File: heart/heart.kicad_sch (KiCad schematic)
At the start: 47 parts

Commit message: [New] Almost complete heart board
Signed-off-by: Homalozoa X <nx.tardis@gmail.com>
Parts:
- added C1, C2: 30pf 10V, Capacitor_SMD:C_0805_2012Metric, symbol Device:C
- added C21, C23: 1uf 10V, Capacitor_SMD:C_0402_1005Metric, symbol Device:C
- added C22, C24: 470pf 10V, Capacitor_SMD:C_0402_1005Metric, symbol Device:C
- added C25, C26: 22nf 10V, Capacitor_SMD:C_0805_2012Metric, symbol Device:C
- added C27: 1nf 2kv, Capacitor_SMD:C_1206_3216Metric, symbol Device:C
- added C28, C29: 4.7nf 2kv, Capacitor_SMD:C_1206_3216Metric, symbol Device:C
- added FB1: 220R, symbol Device:FerriteBead
- added J10: UART_FLASH_ESP, Connector_JST:JST_GH_BM05B-GHS-TBT_1x05-1MP_P1.25mm_Vertical, symbol Connector:Conn_01x05_Female
- added J11: RJ45_LED_Shielded, symbol Connector:RJ45_LED_Shielded
- added Q4, Q5, Q6: FH1404G6, Rolling_Custom:PDFN5X6-8L, symbol Rolling_Custom:WNM6006
- added R10, R11, R12, R13, R14, R33, R6, R7, R8, R9: 0r, Resistor_SMD:R_0402_1005Metric, symbol Device:R_US
- added R15: 499r, Resistor_SMD:R_0402_1005Metric, symbol Device:R_US
- added R22, R23: 10k, Resistor_SMD:R_0402_1005Metric, symbol Device:R_US
- added R24: 12.1k, Resistor_SMD:R_0201_0603Metric, symbol Device:R_US
- added R25, R26, R27, R28: 49.9r, Resistor_SMD:R_0402_1005Metric, symbol Device:R_US
- added R29, R30: 75r, Resistor_SMD:R_0402_1005Metric, symbol Device:R_US
- added R3: 33r, Resistor_SMD:R_0402_1005Metric, symbol Device:R_US
- added R31, R32: 332r, Resistor_SMD:R_0402_1005Metric, symbol Device:R_US
- added R5: 470r, Resistor_SMD:R_0402_1005Metric, symbol Device:R_US
- added T1: H1102NLT, Rolling_Custom:XFMR_H1102NLT, symbol Rolling_Custom:H1102NLT
- added U4: LAN8720A, Package_DFN_QFN:QFN-24-1EP_4x4mm_P0.5mm_EP2.6x2.6mm, symbol Interface_Ethernet:LAN8720A
- added Y1: 25MHz, Crystal:Crystal_SMD_3225-4Pin_3.2x2.5mm, symbol Device:Crystal_GND24
- C3, C4: renamed from C?; footprint Capacitor_SMD:C_0805_2012Metric -> Capacitor_SMD:C_0402_1005Metric
- C5: renamed from C?; value 100uf 10V -> 100uf 6.3V
- gave numbers to parts that had none: 44
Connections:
- net +24V: now also Q4.5; no longer J1.1 (VBUS), J2.1 (VBUS), J3.1 (VBUS), J4.1 (VBUS), J5.1 (VBUS), J6.1 (VBUS), J7.1 (VBUS)
- net +3V3: now also C21.2, C22.2, FB1.1, U4.9 (VDDIO)
- net BOOT0: now also R5.1
- net ESP_DTR: now also J10.1 (Pin_1)
- net ESP_RTS: now also J10.2 (Pin_2)
- net ESP_RXD: now also J10.4 (Pin_4)
- net ESP_TXD: now also R15.2
- net GND: now also J9.2 (-), J9.S1 (SHIELD), J9.S2 (SHIELD), C1.1, C2.1, C21.1, C22.1, C23.1, C24.1, C25.1, C26.1, C28.1, C29.1, J10.5 (Pin_5), J11.11, J11.9, R22.2, R23.2, R24.2, U4.25 (VSS), Y1.2, Y1.4
- net TCAN_INT: now also U1.4 (SENSOR_VP/GPIO36/ADC1_CH0)
- net TCAN_RST: now also U1.26 (ADC2_CH0/GPIO4)
- net TCAN_WKRQ: now also U1.5 (SENSOR_VN/GPIO39/ADC1_CH3)
- net at U1.10 (DAC_1/ADC2_CH8/GPIO25): now also R12.2
- net at U1.11 (DAC_2/ADC2_CH9/GPIO26): now also R13.2
- net at U1.12 (ADC2_CH7/GPIO27): now also R14.2
- net at U1.29 (GPIO5): now also R6.2
- net at U1.30 (GPIO18): now also R7.2
- net at U1.31 (GPIO19): now also R8.2
- net at U1.33 (GPIO21): now also R9.2
- net at U1.36 (GPIO22): now also R10.2
- net at U1.37 (GPIO23): now also R11.2
- net PWRCT_1: now reaches U1.6 (GPIO34/ADC1_CH6)
- net PWRCT_1: now also Q4.4
- net PWRCT_2: now reaches U1.7 (GPIO35/ADC1_CH7)
- net PWRCT_2: now also Q5.4
- net PWRCT_3: now reaches U1.8 (32K_XP/GPIO32/ADC1_CH4)
- net PWRCT_3: now also Q6.4
- net ETH_RXER: now reaches U1.9 (32K_XN/GPIO33/ADC1_CH5)
- net ETH_RXER: now also U4.10 (RXER/PHYAD0)
- net EXT_PWR: now reaches J9.1 (+)
- net EXT_PWR: now also Q5.5, Q6.1, Q6.2, Q6.3
- new net: C27.2, R29.1, R30.1
- new net: R29.2, T1.10
- new net: R3.2, U4.14 (INT/REFCLKO)
- new net: R24.1, U4.24 (RBIAS)
- new net: J11.12, R31.1
- new net: J11.1, T1.16
- new net: J11.10, R32.1
- new net: J11.2, T1.14
- new net: J11.3, T1.11
- new net: J11.6, T1.9
- new net: J10.3 (Pin_3), R15.1
- new net: C26.2, T1.7
- new net: C25.2, T1.2
- new net: R30.2, T1.15
- new net ETH_CLKI: C1.2, U4.5 (XTAL1/CLKIN), Y1.1
- new net ETH_CLKO: C2.2, U4.4 (XTAL2), Y1.3
- new net ETH_LED1: R22.1, R31.2, U4.3 (LED1/REGOFF)
- new net ETH_LED2: R23.1, R32.2, U4.2 (LED2/nINTSEL)
- new net ETH_MDC: R11.1, U4.13 (MDC)
- new net ETH_MDIO: R7.1, U4.12 (MDIO)
- new net ETH_RST_N: R6.1, U4.15 (RST)
- new net ETH_RXN: R25.1, T1.8, U4.22 (RXN)
- new net ETH_RXP: R26.1, T1.6, U4.23 (RXP)
- new net ETH_TXN: R27.1, T1.3, U4.20 (TXN)
- new net ETH_TXP: R28.1, T1.1, U4.21 (TXP)
- new net GNDPWR: C27.1, C28.2, C29.2, R33.2
- new net GNDS: J11.SH, R33.1
- new net PWR_EXPORT: J1.1 (VBUS), J2.1 (VBUS), J3.1 (VBUS), J4.1 (VBUS), J5.1 (VBUS), J6.1 (VBUS), J7.1 (VBUS), Q4.1, Q4.2, Q4.3, Q5.1, Q5.2, Q5.3, Q6.5
- new net RMII_CRS_DV: R14.1, U4.11 (CRS_DV/MODE2)
- new net RMII_REF_CLK: R3.1, R5.2
- new net RMII_RXD0: R12.1, U4.8 (RXD0/MODE0)
- new net RMII_RXD1: R13.1, U4.7 (RXD1/MODE1)
- new net RMII_TXD0: R8.1, U4.17 (TXD0)
- new net RMII_TXD1: R10.1, U4.18 (TXD1)
- new net RMII_TX_EN: R9.1, U4.16 (TXEN)
- new net VDDA: FB1.2, R25.2, R26.2, R27.2, R28.2, U4.1 (VDD2A), U4.19 (VDD1A)
- new net VDDCR: C23.2, C24.2, U4.6 (VDDCR)
- no-connect marks 4 -> 6
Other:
- moved on the sheet: C10, C13, C14, C16, C17, C18, C3, C4, C5, C6, C8, C9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

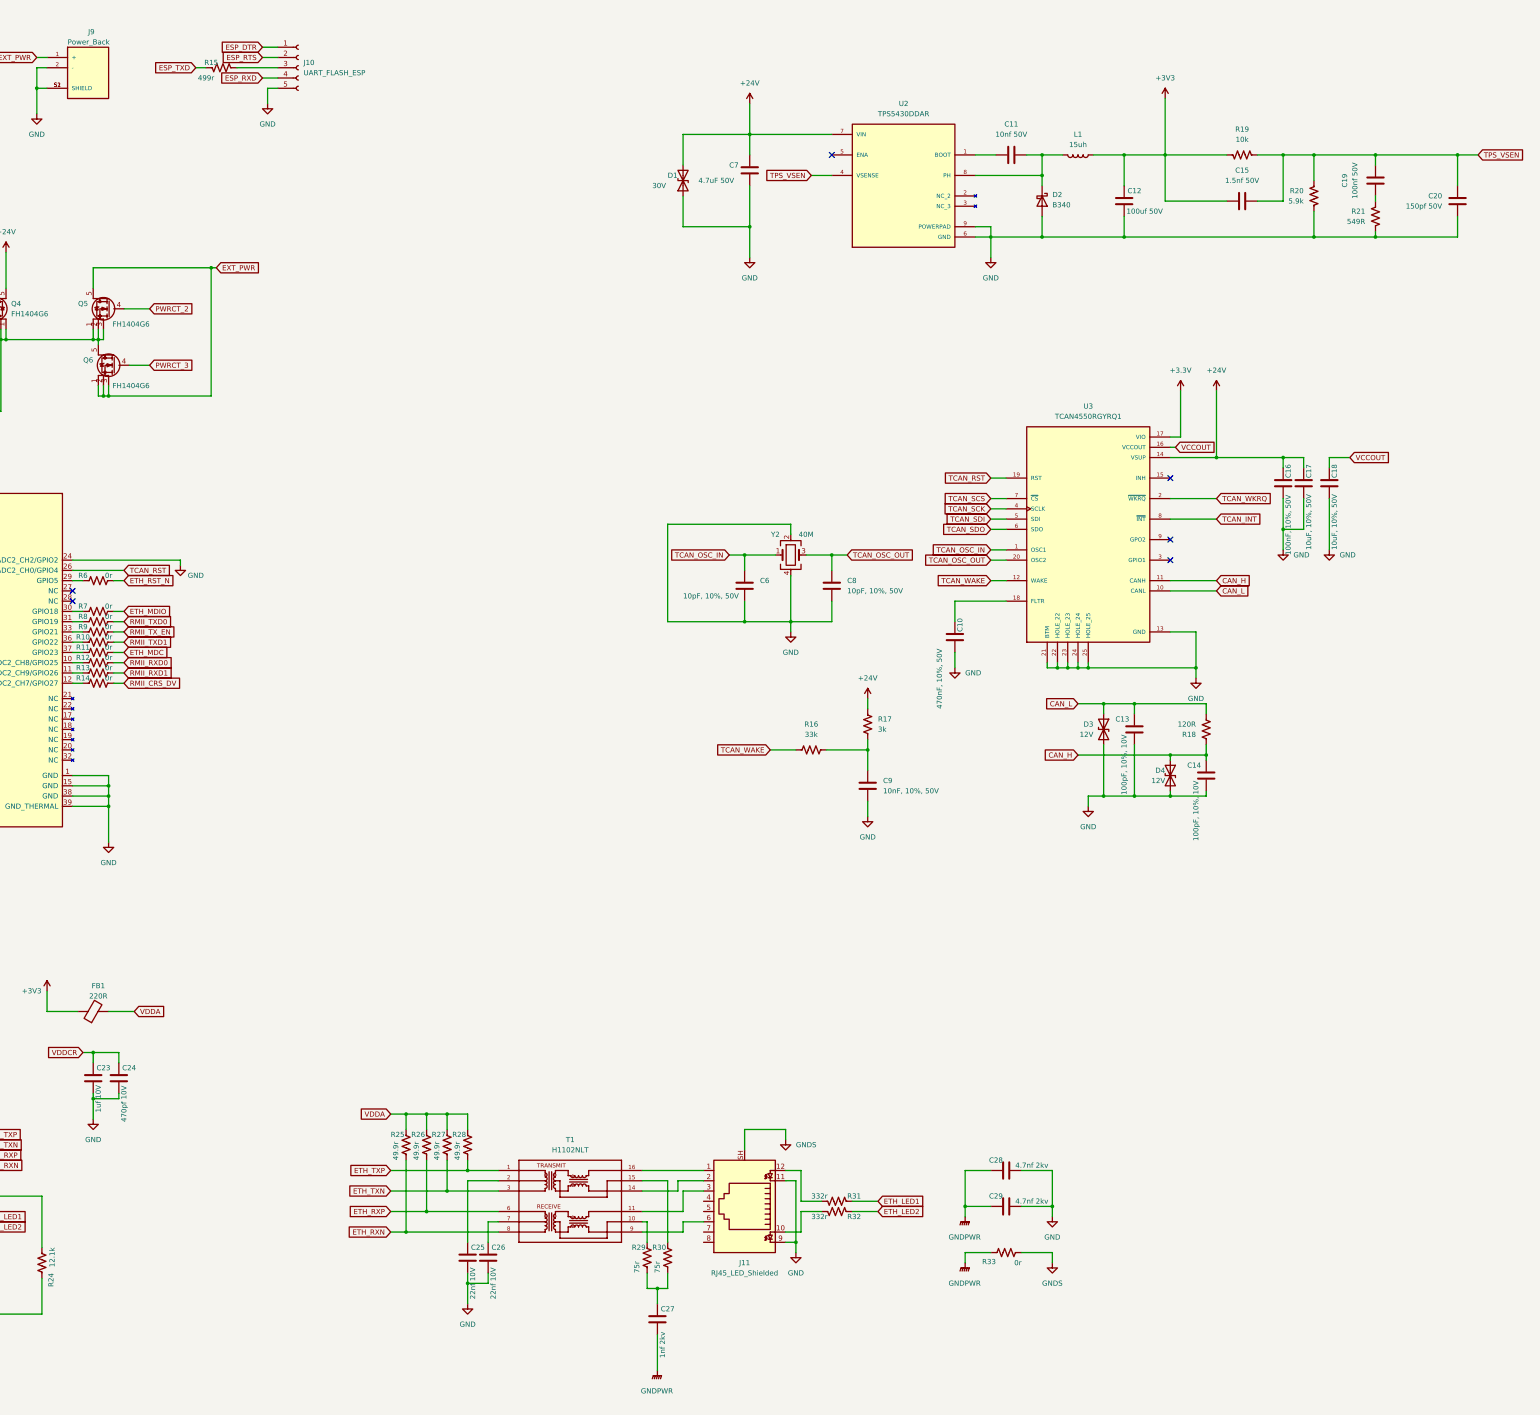
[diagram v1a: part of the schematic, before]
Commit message: [New] Complete heart board
Signed-off-by: Homalozoa X <nx.tardis@gmail.com>
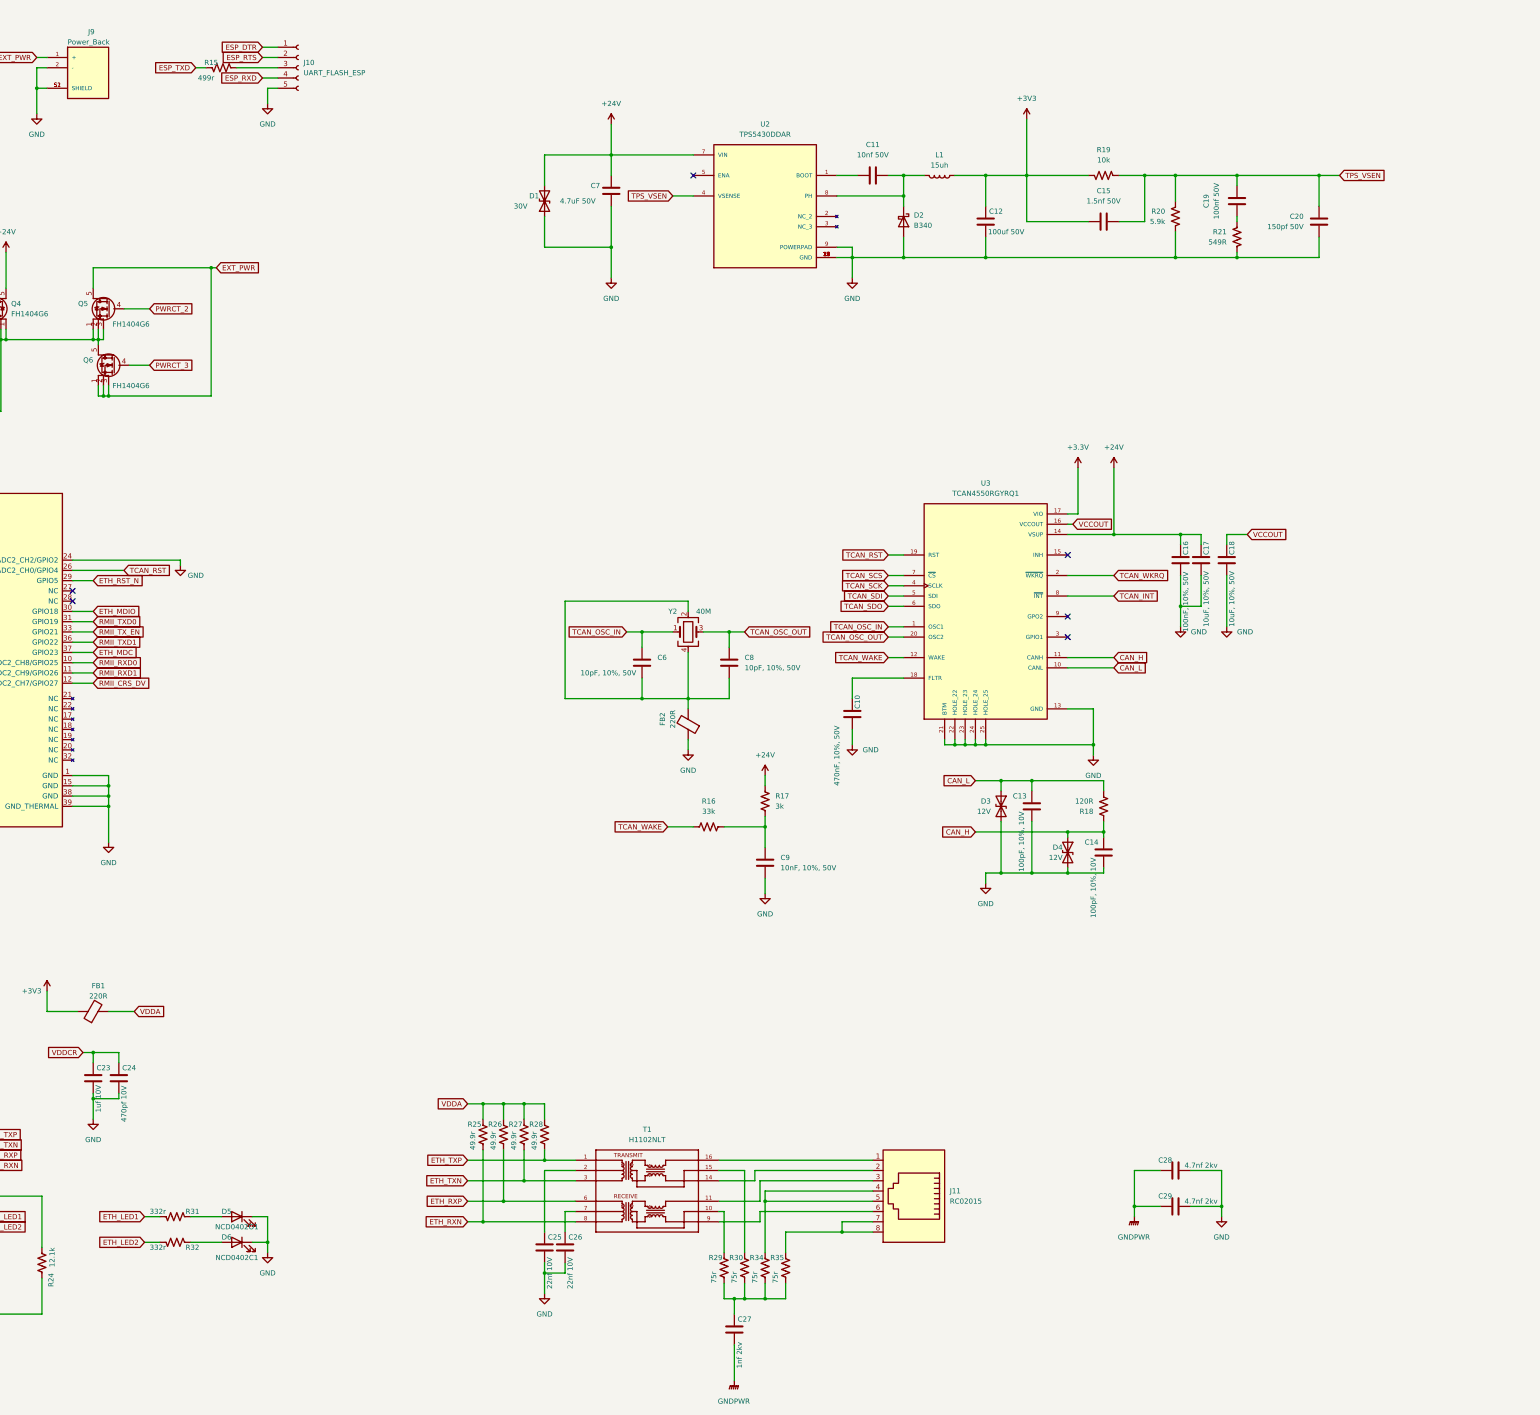
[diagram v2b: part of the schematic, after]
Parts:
- removed J11: RJ45_LED_Shielded, symbol Connector:RJ45_LED_Shielded
- removed R10, R11, R12, R13, R14, R33, R6, R7, R8, R9: 0r, Resistor_SMD:R_0402_1005Metric, symbol Device:R_US
- added D5: NCD0402O1, LED_SMD:LED_0402_1005Metric, symbol Device:LED
- added D6: NCD0402C1, LED_SMD:LED_0402_1005Metric, symbol Device:LED
- added FB2: 220R, Resistor_SMD:R_0603_1608Metric, symbol Device:FerriteBead
- added J11: RC02015, Connector_RJ:RJ45_Molex_0855135013_Vertical, symbol Connector:RJ45
- added R34, R35: 75r, Resistor_SMD:R_0402_1005Metric, symbol Device:R_US
- FB1: footprint (none) -> Resistor_SMD:R_0603_1608Metric
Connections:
- net ETH_LED1: now also R31.1; no longer R31.2
- net ETH_LED2: now also R32.1; no longer R32.2
- net ETH_MDC: now also U1.37 (GPIO23)
- net ETH_MDIO: now also U1.30 (GPIO18)
- net ETH_RST_N: now also U1.29 (GPIO5)
- net GND: now also U2.10 (GND), U2.11 (GND), U2.12 (GND), U2.13 (GND), U2.14 (GND), U2.15 (GND), U2.16 (GND), U2.17 (GND), D5.1 (K), D6.1 (K), FB2.1; no longer C6.1, C8.1, Y2.2, Y2.4
- net RMII_CRS_DV: now also U1.12 (ADC2_CH7/GPIO27)
- net RMII_RXD0: now also U1.10 (DAC_1/ADC2_CH8/GPIO25)
- net RMII_RXD1: now also U1.11 (DAC_2/ADC2_CH9/GPIO26)
- net RMII_TXD0: now also U1.31 (GPIO19)
- net RMII_TXD1: now also U1.36 (GPIO22)
- net RMII_TX_EN: now also U1.33 (GPIO21)
- net at C27.2, R29.1, R30.1: now also R34.1, R35.1
- net at T1.16: now also J11.1
- net at T1.14: now also J11.2
- net at T1.11: now also J11.3
- net at T1.9: now also J11.6
- new net: D6.2 (A), R32.2
- new net: C6.1, C8.1, FB2.2, Y2.2, Y2.4
- new net: D5.2 (A), R31.2
- new net: J11.4, J11.5, R34.2
- new net: J11.7, J11.8, R35.2
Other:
- moved on the sheet: C10, C11, C12, C13, C14, C15, C16, C17, C18, C19, C20, C25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
